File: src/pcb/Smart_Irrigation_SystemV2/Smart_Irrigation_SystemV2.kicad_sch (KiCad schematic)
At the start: 126 parts, among them J1 USB_C_Receptacle_USB2.0_16P, J10 I2C, J11 I2C, J12 AudioJack3, J14 SolarPanel, J2 FPC_Connector, J3 AudioJack3, J4 AudioJack3, J5 AudioJack3, J6 I2C, J7 AudioJack3, J8 AudioJack3, J9 Battary Connection, Q1 MUN5211DW1, Q2 FDN340P, Q3 AO3400A, SW1 IO0 Switch, SW2 EN Switch, SW3 SW_Push, SW4 SW_Push, SW5 SW_Push, SW6 SW_Push, U1 CP2102N-Axx-xQFN28, U10 ADS1115IDGS, U2 ESP32-WROOM-32, U3 ADS1115IDGS, U4 DS3231MZ, U5 TLV62568ADRL, U6 SN74LVC245APW, U7 TP4056-42-ESOP8, U8 TPS63001, U9 AT24CS32-SSHM

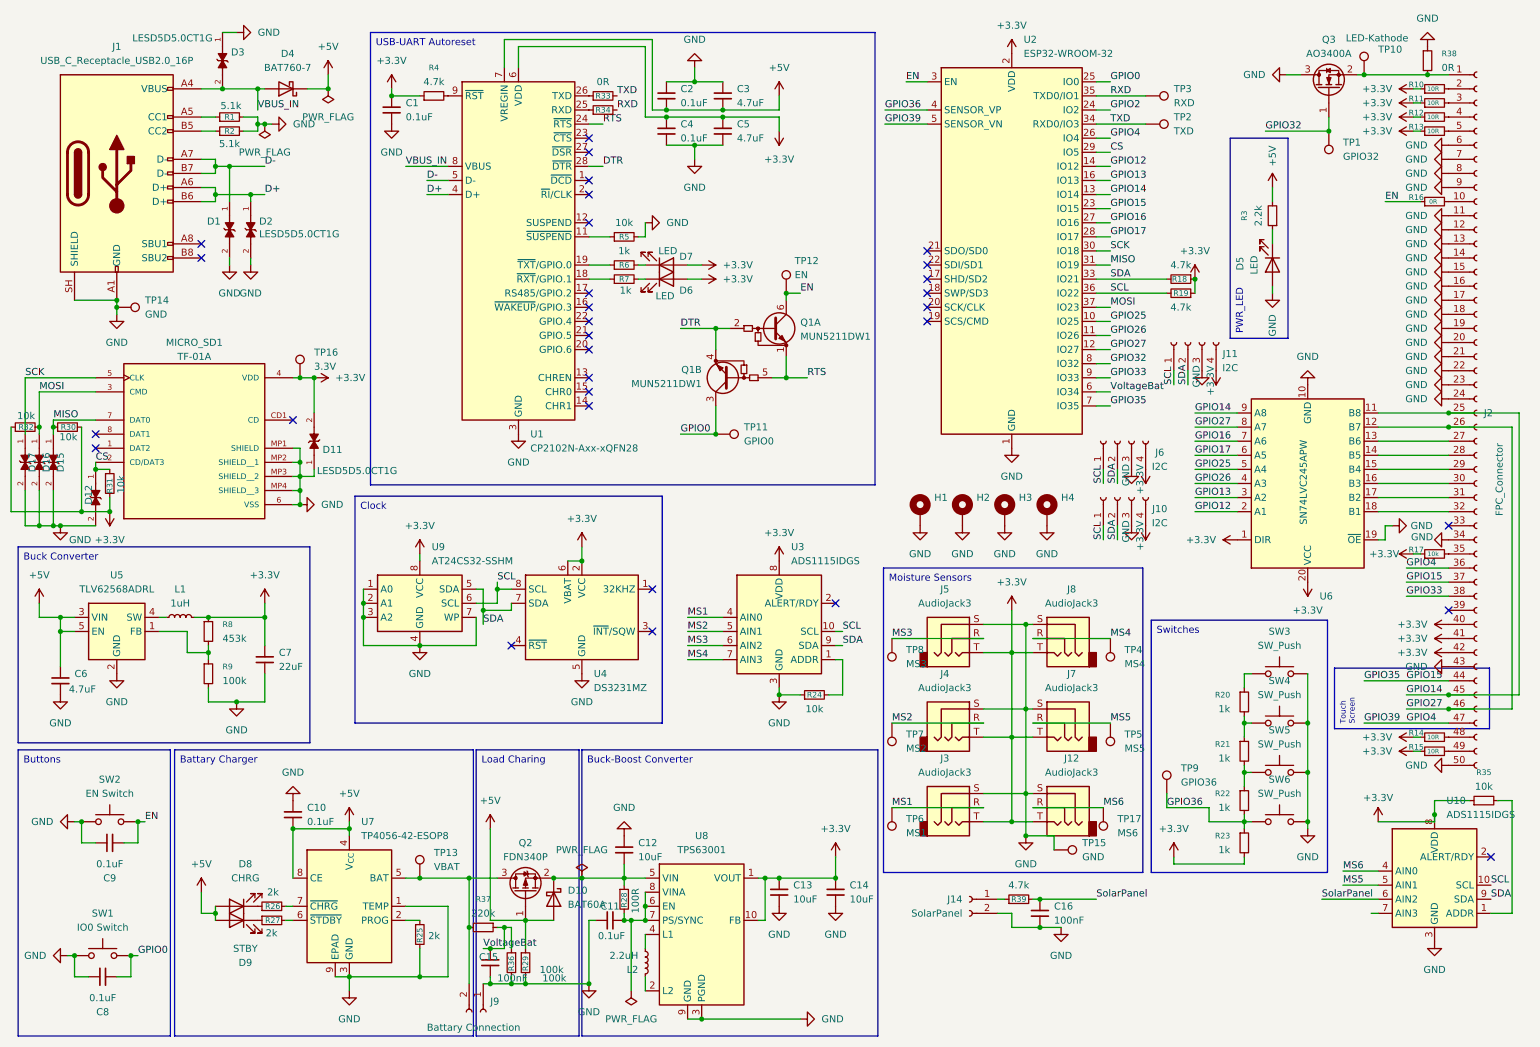
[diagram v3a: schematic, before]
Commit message: added Solar, GPIO Expander
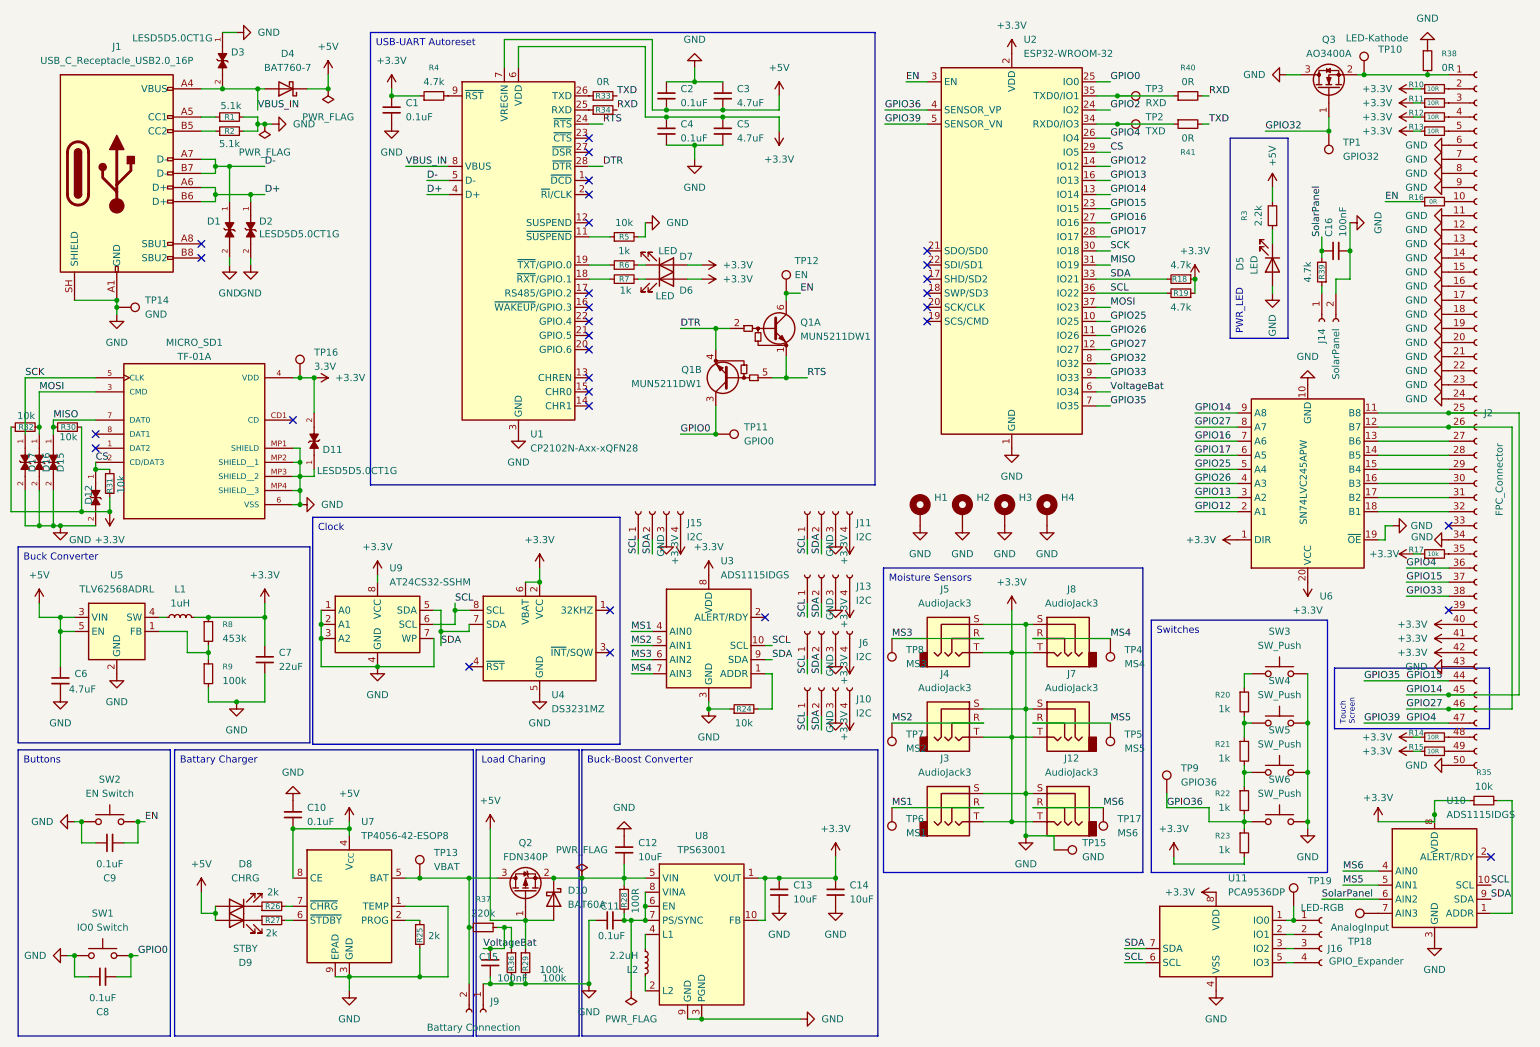
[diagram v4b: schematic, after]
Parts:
- added J13, J15: I2C, Connector_JST:JST_EH_B4B-EH-A_1x04_P2.50mm_Vertical, symbol Connector:Conn_01x04_Socket
- added J16: GPIO_Expander, Connector_PinSocket_2.54mm:PinSocket_1x04_P2.54mm_Vertical, symbol Connector:Conn_01x04_Socket
- added R40, R41: 0R, Resistor_SMD:R_0805_2012Metric, symbol Device:R_Small
- added TP18: AnalogInput, TestPoint:TestPoint_Pad_D1.5mm, symbol Connector:TestPoint
- added TP19: LED-RGB, TestPoint:TestPoint_Pad_D4.0mm, symbol Connector:TestPoint
- added U11: PCA9536DP, Package_SO:TSSOP-8_3x3mm_P0.65mm, symbol Interface_Expansion:PCA9536DP
- C16: footprint (none) -> Capacitor_SMD:C_0805_2012Metric; JLCPCB Part Number (none) -> C29926
- J10, J11, J6: footprint Connector_PinSocket_2.54mm:PinSocket_1x04_P2.54mm_Vertical -> Connector_JST:JST_EH_B4B-EH-A_1x04_P2.50mm_Vertical
- J14: footprint (none) -> Connector_JST:JST_PH_B2B-PH-K_1x02_P2.00mm_Vertical
- R38: JLCPCB Part Number (none) -> C17477
- R39: footprint Resistor_THT:R_Array_SIP4 -> Resistor_SMD:R_0805_2012Metric; JLCPCB Part Number (none) -> C17673
- TP17: footprint Relay_THT:Relay_DPDT_Schrack-RT2-FormC_RM5mm -> TestPoint:TestPoint_Pad_D1.5mm
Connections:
- net +3.3V: now also J13.4 (Pin_4), J15.4 (Pin_4), U11.8 (VDD)
- net GND: now also J13.3 (Pin_3), J15.3 (Pin_3), U11.4 (VSS)
- net RXD: now also R40.2; no longer TP3.1, U2.35 (TXD0/IO1)
- net SCL: now also J13.1 (Pin_1), J15.1 (Pin_1), U11.6 (SCL)
- net SDA: now also J13.2 (Pin_2), J15.2 (Pin_2), U11.7 (SDA)
- net TXD: now also R41.2; no longer TP2.1, U2.34 (RXD0/IO3)
- net at U10.7 (AIN3): now also TP18.1
- new net: R40.1, TP3.1, U2.35 (TXD0/IO1)
- new net: R41.1, TP2.1, U2.34 (RXD0/IO3)
- new net: J16.1 (Pin_1), TP19.1, U11.1 (IO0)
- new net: J16.2 (Pin_2), U11.2 (IO1)
- new net: J16.3 (Pin_3), U11.3 (IO2)
- new net: J16.4 (Pin_4), U11.5 (IO3)
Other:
- moved on the sheet: C16, J10, J11, J14, J6, R24, R39, TP2, TP3, U3, U4, U9

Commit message: layout of the pcb - wiring without gnd and power plane
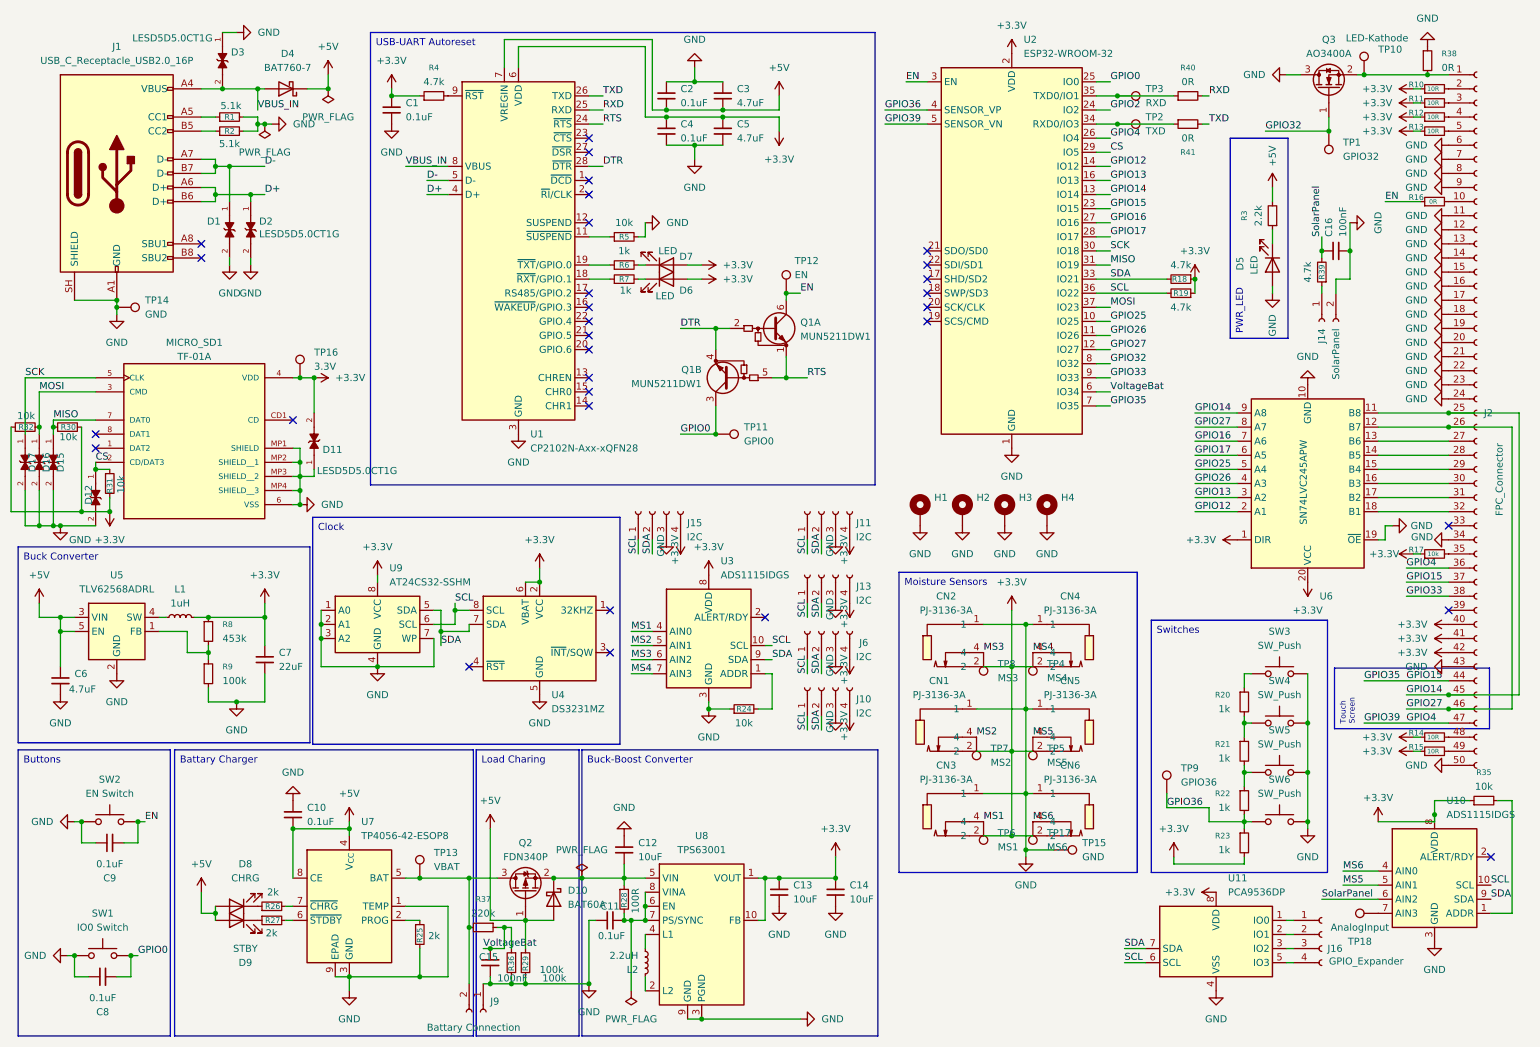
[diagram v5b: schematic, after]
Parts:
- removed J12, J3, J4, J5, J7, J8: AudioJack3, Test:AUDIO-TH_PJ-3136-3A, symbol Connector_Audio:AudioJack3
- removed R33, R34: 0R, Resistor_SMD:R_0805_2012Metric, symbol Device:R_Small
- removed TP19: LED-RGB, TestPoint:TestPoint_Pad_D4.0mm, symbol Connector:TestPoint
- added CN1, CN2, CN3, CN4, CN5, CN6: PJ-3136-3A, Test:AUDIO-TH_PJ-3136-3A, symbol easyeda2kicad:PJ-3136-3A
- R40, R41: footprint Resistor_SMD:R_0805_2012Metric -> Resistor_SMD:R_1206_3216Metric
- SW3, SW4, SW5, SW6: footprint Test:SW-TH_CPG151101D9X -> Button_Switch_THT:SW_PUSH_6mm_H4.3mm
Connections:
- net +3.3V: now also CN1.2, CN2.2, CN3.2, CN4.2, CN5.2, CN6.2
- net GND: now also CN1.1, CN2.1, CN3.1, CN4.1, CN5.1, CN6.1
- net MS1: now also CN3.4
- net MS2: now also CN1.4
- net MS3: now also CN2.4
- net MS4: now also CN4.4
- net MS5: now also CN5.4
- net MS6: now also CN6.4
- net RXD: now also U1.25 (RXD)
- net TXD: now also U1.26 (TXD)
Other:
- moved on the sheet: TP6, TP8

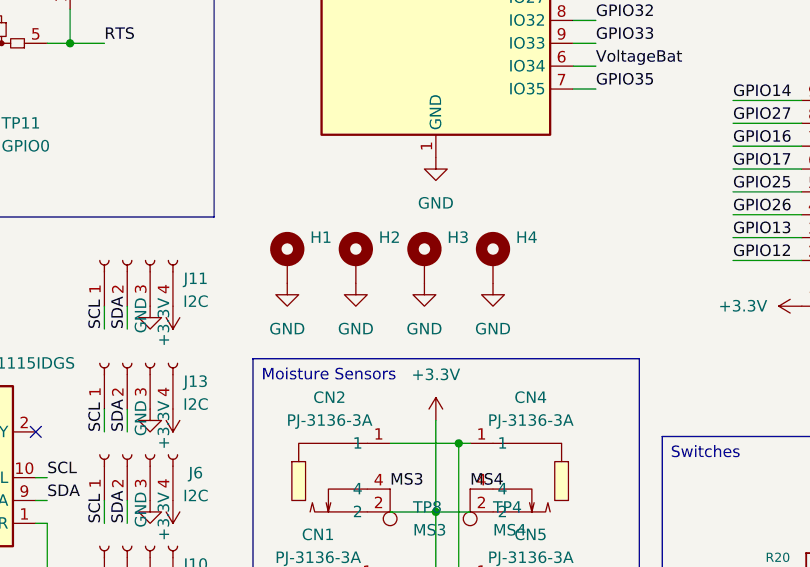
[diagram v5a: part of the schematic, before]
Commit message: added 3D models to the parts and modified shape of pcb
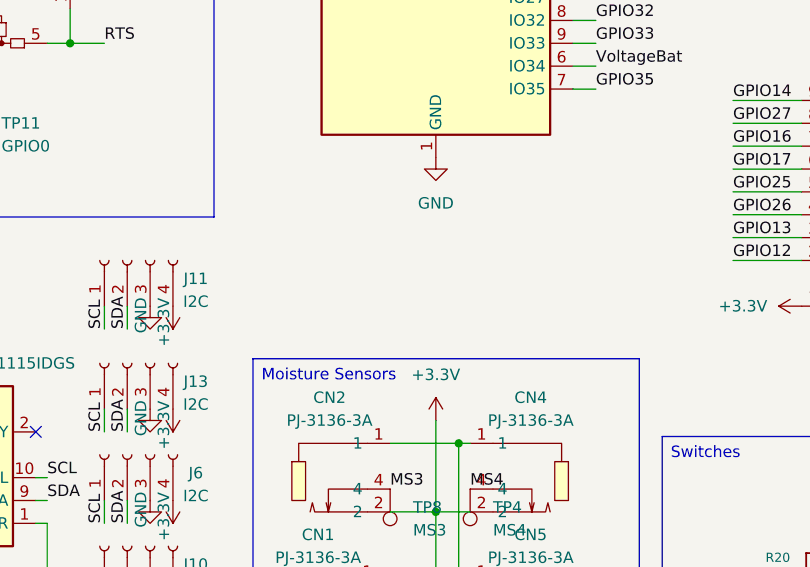
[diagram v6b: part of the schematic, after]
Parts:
- removed H1, H2, H3, H4: MountingHole_Pad, MountingHole:MountingHole_3.2mm_M3_DIN965_Pad, symbol Mechanical:MountingHole_Pad
- CN1, CN2, CN3, CN4, CN5, CN6: footprint Test:AUDIO-TH_PJ-3136-3A -> C707248:AUDIO-TH_PJ-3136-3A
- J1: footprint Connector_USB:USB_C_Receptacle_HRO_TYPE-C-31-M-12 -> C5337088:USB-C-SMD_TYPE-C-31-M-12A
- L1: footprint Inductor_SMD:L_7.3x7.3_H3.5 -> C726315:IND-SMD_L7.1-W6.6
- L2: footprint Inductor_SMD:L_7.3x7.3_H3.5 -> C128686:IND-SMD_L6.6-W6.6
- MICRO_SD1: footprint TF-01A:TF-01A -> C91145:TF-SMD_TF-01A
- R40, R41: JLCPCB Part Number C17477 -> C17888
- SW1, SW2: footprint Test:KEY-SMD_4P-L6.0-W6.0-P3.90-LS9.0 -> C83206:KEY-SMD_4P-L6.0-W6.0-P3.90-LS9.0
- SW3, SW4, SW5, SW6: JLCPCB Part Number C49234238 -> (none)
- U7: footprint Package_SO:SOIC-8-1EP_3.9x4.9mm_P1.27mm_EP2.41x3.3mm_ThermalVias -> C16581:ESOP-8_L4.9-W3.9-P1.27-LS6.0-BL-EP
- U8: footprint Package_SON:Texas_DRC0010J_ThermalVias -> C28060:VSON-10_L3.0-W3.0-P0.50-TL-EP_TPS62410DRCR
